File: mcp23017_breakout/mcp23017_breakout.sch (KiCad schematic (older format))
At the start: 10 parts, among them U1 address_sel, U2 address_sel, U3 address_sel, U4 MCP23017

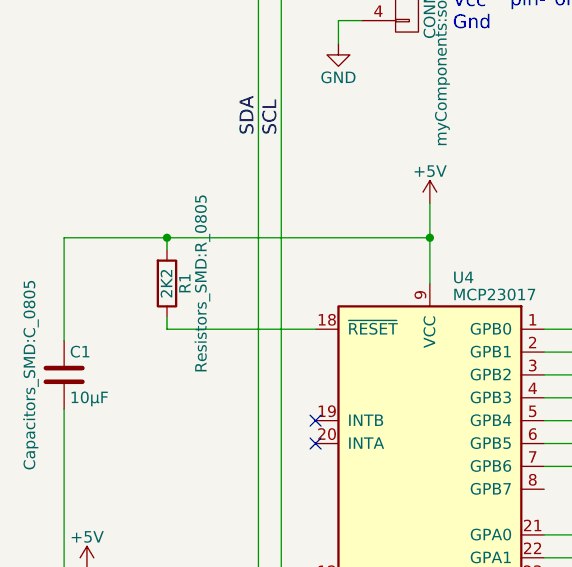
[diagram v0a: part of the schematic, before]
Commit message: switched reset pullups from 2K2 to 10K
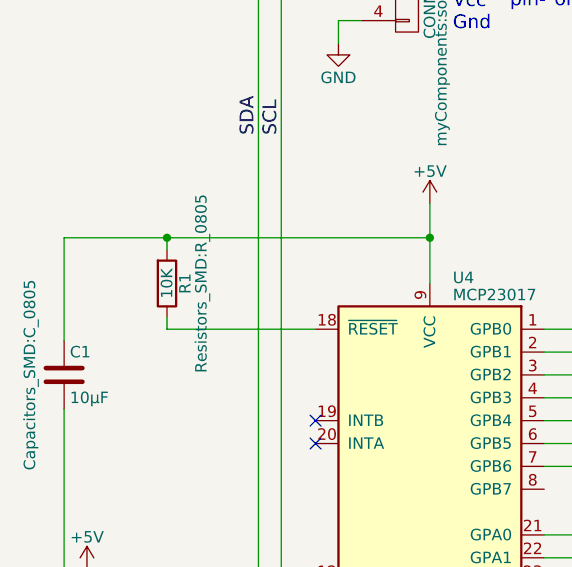
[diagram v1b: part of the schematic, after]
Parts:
- R1: value 2K2 -> 10K
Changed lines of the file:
@@
 $EndComp
 $Comp
-L +5V #PWR4
+L +5V #PWR01
 U 1 1 58E29592
 P 4500 2400
-F 0 "#PWR4" H 4500 2250 50  0001 C CNN
+F 0 "#PWR01" H 4500 2250 50  0001 C CNN
 F 1 "+5V" H 4500 2540 50  0000 C CNN
 F 2 "" H 4500 2400 50  0000 C CNN
@@
 $EndComp
 $Comp
-L GND #PWR5
+L GND #PWR02
 U 1 1 58E295D6
 P 4500 5400
-F 0 "#PWR5" H 4500 5150 50  0001 C CNN
+F 0 "#PWR02" H 4500 5150 50  0001 C CNN
 F 1 "GND" H 4500 5250 50  0000 C CNN
 F 2 "" H 4500 5400 50  0000 C CNN
@@
 $EndComp
 $Comp
-L GND #PWR7
+L GND #PWR03
 U 1 1 58E39CFA
 P 7750 5750
-F 0 "#PWR7" H 7750 5500 50  0001 C CNN
+F 0 "#PWR03" H 7750 5500 50  0001 C CNN
 F 1 "GND" H 7750 5600 50  0000 C CNN
 F 2 "" H 7750 5750 50  0000 C CNN
@@
 $EndComp
 $Comp
-L +5V #PWR6
+L +5V #PWR04
 U 1 1 58E39D32
 P 7550 5750
-F 0 "#PWR6" H 7550 5600 50  0001 C CNN
+F 0 "#PWR04" H 7550 5600 50  0001 C CNN
 F 1 "+5V" H 7550 5890 50  0000 C CNN
 F 2 "" H 7550 5750 50  0000 C CNN
@@
 $EndComp
 $Comp
-L +5V #PWR2
+L +5V #PWR05
 U 1 1 58E561FB
 P 4100 1200
-F 0 "#PWR2" H 4100 1050 50  0001 C CNN
+F 0 "#PWR05" H 4100 1050 50  0001 C CNN
 F 1 "+5V" H 4100 1340 50  0000 C CNN
 F 2 "" H 4100 1200 50  0000 C CNN
@@
 $EndComp
 $Comp
-L GND #PWR3
+L GND #PWR06
 U 1 1 58E5624E
 P 4100 1700
-F 0 "#PWR3" H 4100 1450 50  0001 C CNN
+F 0 "#PWR06" H 4100 1450 50  0001 C CNN
 F 1 "GND" H 4100 1550 50  0000 C CNN
 F 2 "" H 4100 1700 50  0000 C CNN
@@
 P 3350 2750
 F 0 "R1" V 3430 2750 50  0000 C CNN
-F 1 "2K2" V 3350 2750 50  0000 C CNN
+F 1 "10K" V 3350 2750 50  0000 C CNN
 F 2 "Resistors_SMD:R_0805" V 3500 2750 50  0000 C CNN
 F 3 "" H 3350 2750 50  0000 C CNN
@@
 	3550 4200 3500 4200
 $Comp
-L +5V #PWR1
+L +5V #PWR07
 U 1 1 58E8271F
 P 3000 4000
-F 0 "#PWR1" H 3000 3850 50  0001 C CNN
+F 0 "#PWR07" H 3000 3850 50  0001 C CNN
 F 1 "+5V" H 3000 4140 50  0000 C CNN
 F 2 "" H 3000 4000 50  0000 C CNN

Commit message: more fixes :-s
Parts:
- renumbered U1 to A0, U2 to A1, U3 to A2
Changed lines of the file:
@@
 	3550 4350 4000 4350
 $Comp
-L address_sel U1
+L address_sel A0
 U 1 1 58E81F3D
 P 3250 4200
-F 0 "U1" H 3250 4025 60  0000 C CNN
+F 0 "A0" H 3250 4025 60  0000 C CNN
 F 1 "address_sel" H 3250 4375 60  0000 C CNN
 F 2 "myComponents:addr_jumper" H 3250 4200 60  0001 C CNN
@@
 $EndComp
 $Comp
-L address_sel U2
+L address_sel A1
 U 1 1 58E82010
 P 3250 4600
-F 0 "U2" H 3250 4425 60  0000 C CNN
+F 0 "A1" H 3250 4425 60  0000 C CNN
 F 1 "address_sel" H 3250 4775 60  0000 C CNN
 F 2 "myComponents:addr_jumper" H 3250 4600 60  0001 C CNN
@@
 $EndComp
 $Comp
-L address_sel U3
+L address_sel A2
 U 1 1 58E82047
 P 3250 5000
-F 0 "U3" H 3250 4825 60  0000 C CNN
+F 0 "A2" H 3250 4825 60  0000 C CNN
 F 1 "address_sel" H 3250 5175 60  0000 C CNN
 F 2 "myComponents:addr_jumper" H 3250 5000 60  0001 C CNN
